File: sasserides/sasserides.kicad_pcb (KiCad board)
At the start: 2 copper layers, 170 x 80 mm, 128 parts, among them J1 Conn_02x16_Odd_Even, Q1 2N7002

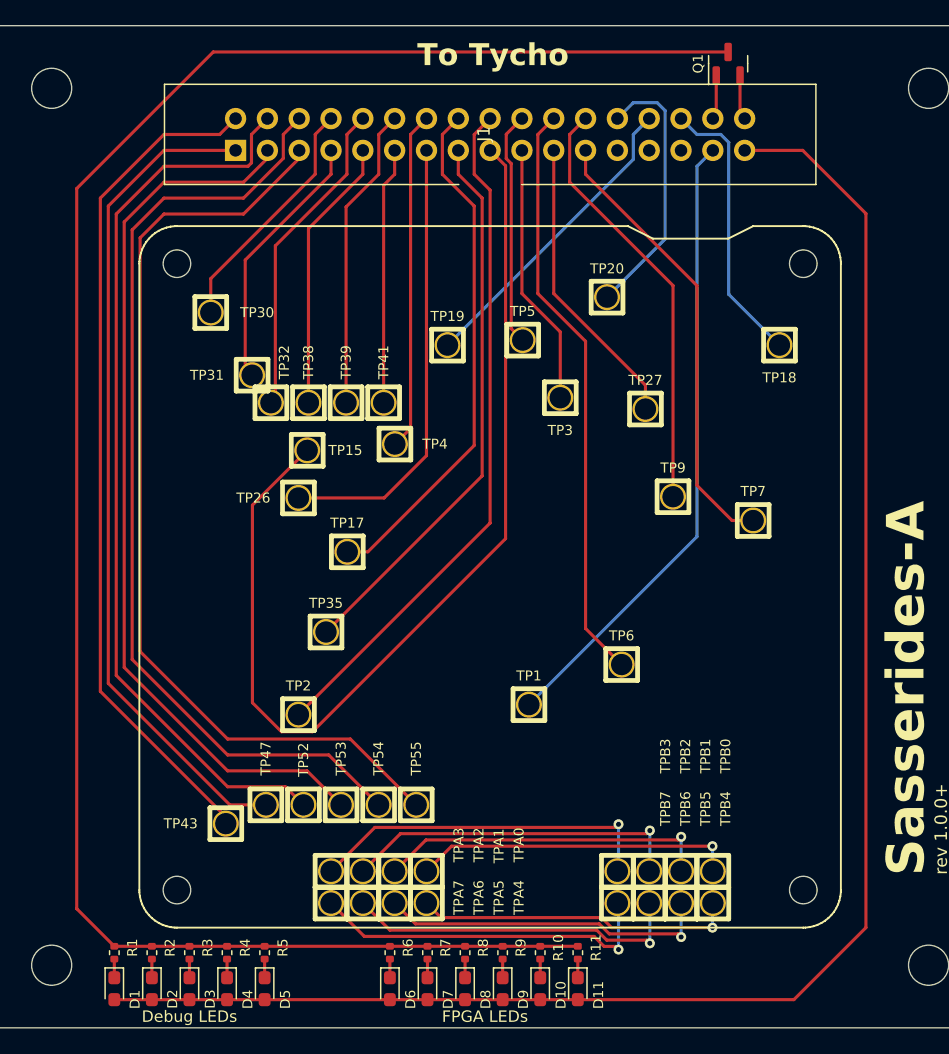
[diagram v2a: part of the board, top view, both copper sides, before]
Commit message: Move Q1 closer to LEDs.
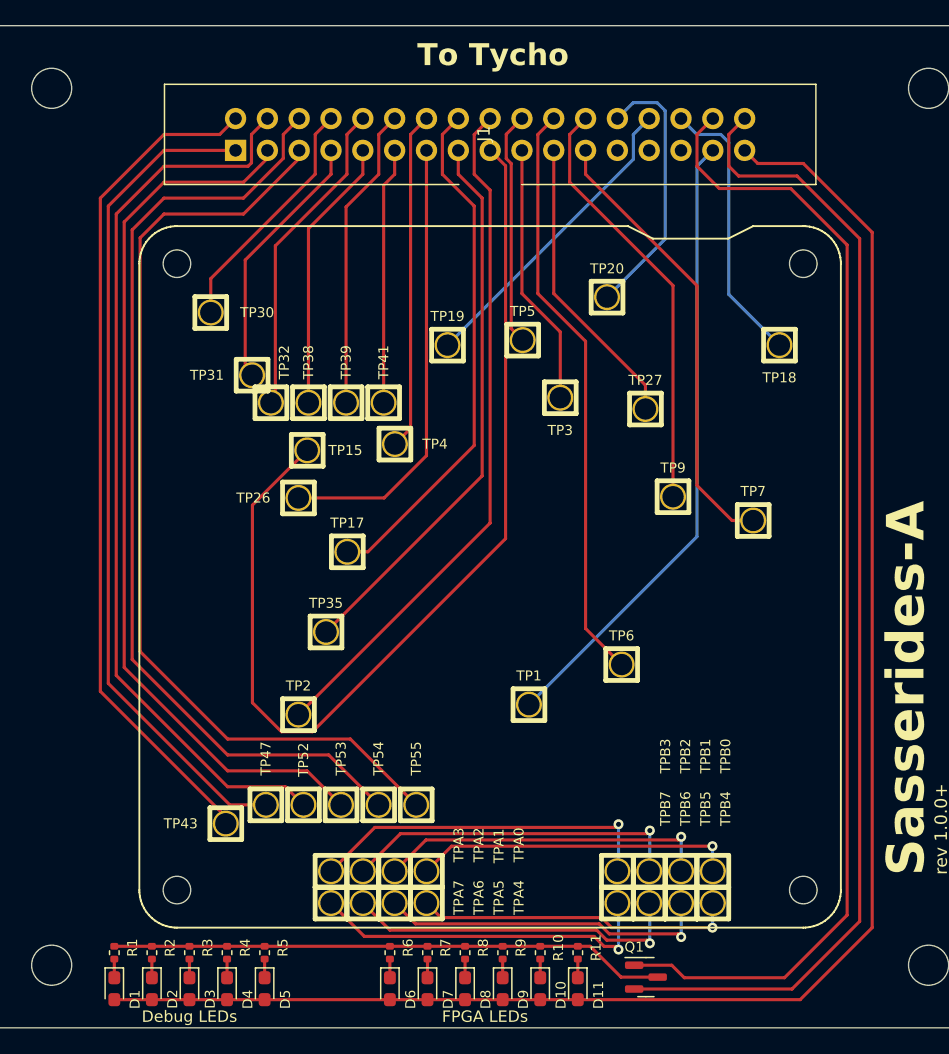
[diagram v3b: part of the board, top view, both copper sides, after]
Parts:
- moved Q1 73.2 mm to (112.4, 135.9), turned to 0 degrees
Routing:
- net Net-(Q1-D): track 155.2 -> 44.4 mm
- net REF_LED_EN: track 3.55 -> 91.9 mm
- net GND: track 3.59 -> 91.9 mm
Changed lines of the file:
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@@
   )
   (footprint "Package_TO_SOT_SMD:SOT-23" (layer "F.Cu")
-    (at 119 63.0375 90)
+    (at 112.4375 135.95)
     (descr "SOT, 3 Pin (https://www.jedec.org/system/files/docs/to-236h.pdf variant AB), generated with kicad-footprint-generator ipc_gullwing_generator.py")
     (tags "SOT TO_SOT_SMD")
@@
     (property "ki_keywords" "N-Channel Switching MOSFET")
     (attr smd)
-    (fp_text reference "Q1" (at 0 -2.4 90) (layer "F.SilkS")
-        (effects (font (size 0.8 0.8) (thickness 0.15)))
-    )
-    (fp_text value "2N7002" (at 0 2.4 90) (layer "F.Fab") hide
+    (fp_text reference "Q1" (at -0.9375 -2.4) (layer "F.SilkS")
+        (effects (font (size 0.8 0.8) (thickness 0.15)))
+    )
+    (fp_text value "2N7002" (at 0 2.4) (layer "F.Fab") hide
         (effects (font (size 1 1) (thickness 0.15)))
     )
-    (fp_text user "${REFERENCE}" (at 0 0 90) (layer "F.Fab")
+    (fp_text user "${REFERENCE}" (at 0 0) (layer "F.Fab")
         (effects (font (size 0.32 0.32) (thickness 0.05)))
     )
@@
     (fp_line (start 0.65 1.45) (end -0.65 1.45)
       (stroke (width 0.1) (type solid)) (layer "F.Fab"))
-    (pad "1" smd roundrect (at -0.9375 -0.95 90) (size 1.475 0.6) (layers "F.Cu" "F.Paste" "F.Mask") (roundrect_rratio 0.25)
+    (pad "1" smd roundrect (at -0.9375 -0.95) (size 1.475 0.6) (layers "F.Cu" "F.Paste" "F.Mask") (roundrect_rratio 0.25)
       (net 44 "REF_LED_EN") (pinfunction "G") (pintype "input"))
-    (pad "2" smd roundrect (at -0.9375 0.95 90) (size 1.475 0.6) (layers "F.Cu" "F.Paste" "F.Mask") (roundrect_rratio 0.25)
+    (pad "2" smd roundrect (at -0.9375 0.95) (size 1.475 0.6) (layers "F.Cu" "F.Paste" "F.Mask") (roundrect_rratio 0.25)
       (net 45 "GND") (pinfunction "S") (pintype "passive"))
-    (pad "3" smd roundrect (at 0.9375 0 90) (size 1.475 0.6) (layers "F.Cu" "F.Paste" "F.Mask") (roundrect_rratio 0.25)
+    (pad "3" smd roundrect (at 0.9375 0) (size 1.475 0.6) (layers "F.Cu" "F.Paste" "F.Mask") (roundrect_rratio 0.25)
       (net 46 "Net-(Q1-D)") (pinfunction "D") (pintype "passive"))
     (model "${KICAD6_3DMODEL_DIR}/Package_TO_SOT_SMD.3dshapes/SOT-23.wrl"
@@
   )
   (segment (start 70 136) (end 70 134.51) (width 0.25) (layer "F.Cu") (net 1))
-  (segment (start 124.25 137.75) (end 130 132) (width 0.25) (layer "F.Cu") (net 2))
-  (segment (start 124.955 69.955) (end 120.32 69.955) (width 0.25) (layer "F.Cu") (net 2))
-  (segment (start 70 137.75) (end 124.25 137.75) (width 0.25) (layer "F.Cu") (net 2))
-  (segment (start 130 132) (end 130 75) (width 0.25) (layer "F.Cu") (net 2))
-  (segment (start 130 75) (end 124.955 69.955) (width 0.25) (layer "F.Cu") (net 2))
+  (segment (start 130.5 76.5) (end 125 71) (width 0.25) (layer "F.Cu") (net 2))
+  (segment (start 124.75 137.75) (end 130.5 132) (width 0.25) (layer "F.Cu") (net 2))
+  (segment (start 121.365 71) (end 120.32 69.955) (width 0.25) (layer "F.Cu") (net 2))
+  (segment (start 125 71) (end 121.365 71) (width 0.25) (layer "F.Cu") (net 2))
+  (segment (start 130.5 132) (end 130.5 76.5) (width 0.25) (layer "F.Cu") (net 2))
+  (segment (start 70 137.75) (end 124.75 137.75) (width 0.25) (layer "F.Cu") (net 2))
   (segment (start 73 136) (end 73 134.51) (width 0.25) (layer "F.Cu") (net 3))
   (segment (start 76 136) (end 76 134.51) (width 0.25) (layer "F.Cu") (net 4))
@@
   (segment (start 117.78 69.955) (end 116.51 71.225) (width 0.25) (layer "B.Cu") (net 43))
   (segment (start 116.51 100.79) (end 103.1 114.2) (width 0.25) (layer "B.Cu") (net 43))
-  (segment (start 118.05 63.975) (end 118.05 67.145) (width 0.25) (layer "F.Cu") (net 44))
-  (segment (start 118.05 67.145) (end 117.78 67.415) (width 0.25) (layer "F.Cu") (net 44))
-  (segment (start 119.95 67.045) (end 120.32 67.415) (width 0.25) (layer "F.Cu") (net 45))
-  (segment (start 119.95 63.975) (end 119.95 67.045) (width 0.25) (layer "F.Cu") (net 45))
-  (segment (start 67 130.49) (end 70 133.49) (width 0.25) (layer "F.Cu") (net 46))
-  (segment (start 67 73) (end 67 130.49) (width 0.25) (layer "F.Cu") (net 46))
-  (segment (start 77.9 62.1) (end 67 73) (width 0.25) (layer "F.Cu") (net 46))
+  (segment (start 116.515 71.22) (end 118.295 73) (width 0.25) (layer "F.Cu") (net 44))
+  (segment (start 123.5 136) (end 115.5 136) (width 0.25) (layer "F.Cu") (net 44))
+  (segment (start 118.295 73) (end 124 73) (width 0.25) (layer "F.Cu") (net 44))
+  (segment (start 116.515 68.68) (end 116.515 71.22) (width 0.25) (layer "F.Cu") (net 44))
+  (segment (start 117.78 67.415) (end 116.515 68.68) (width 0.25) (layer "F.Cu") (net 44))
+  (segment (start 128.5 77.5) (end 128.5 131) (width 0.25) (layer "F.Cu") (net 44))
+  (segment (start 114.5 135) (end 111.5 135) (width 0.25) (layer "F.Cu") (net 44))
+  (segment (start 124 73) (end 128.5 77.5) (width 0.25) (layer "F.Cu") (net 44))
+  (segment (start 115.5 136) (end 114.5 135) (width 0.25) (layer "F.Cu") (net 44))
+  (segment (start 128.5 131) (end 123.5 136) (width 0.25) (layer "F.Cu") (net 44))
+  (segment (start 119.055 71.22) (end 119.055 68.68) (width 0.25) (layer "F.Cu") (net 45))
+  (segment (start 111.5 136.9) (end 124.1 136.9) (width 0.25) (layer "F.Cu") (net 45))
+  (segment (start 124.1 136.9) (end 129.5 131.5) (width 0.25) (layer "F.Cu") (net 45))
+  (segment (start 119.055 68.68) (end 120.32 67.415) (width 0.25) (layer "F.Cu") (net 45))
+  (segment (start 124.5 72) (end 119.835 72) (width 0.25) (layer "F.Cu") (net 45))
+  (segment (start 129.5 131.5) (end 129.5 77) (width 0.25) (layer "F.Cu") (net 45))
+  (segment (start 119.835 72) (end 119.055 71.22) (width 0.25) (layer "F.Cu") (net 45))
+  (segment (start 129.5 77) (end 124.5 72) (width 0.25) (layer "F.Cu") (net 45))
+  (segment (start 113.375 135.95) (end 110.45 135.95) (width 0.25) (layer "F.Cu") (net 46))
+  (segment (start 107.99 133.49) (end 107 133.49) (width 0.25) (layer "F.Cu") (net 46))
   (segment (start 107 133.49) (end 70 133.49) (width 0.25) (layer "F.Cu") (net 46))
-  (segment (start 119 62.1) (end 77.9 62.1) (width 0.25) (layer "F.Cu") (net 46))
+  (segment (start 110.45 135.95) (end 107.99 133.49) (width 0.25) (layer "F.Cu") (net 46))
   (segment (start 96.92 125.5) (end 117.75 125.5) (width 0.25) (layer "F.Cu") (net 47))
   (segment (start 94.92 127.5) (end 96.92 125.5) (width 0.25) (layer "F.Cu") (net 47))

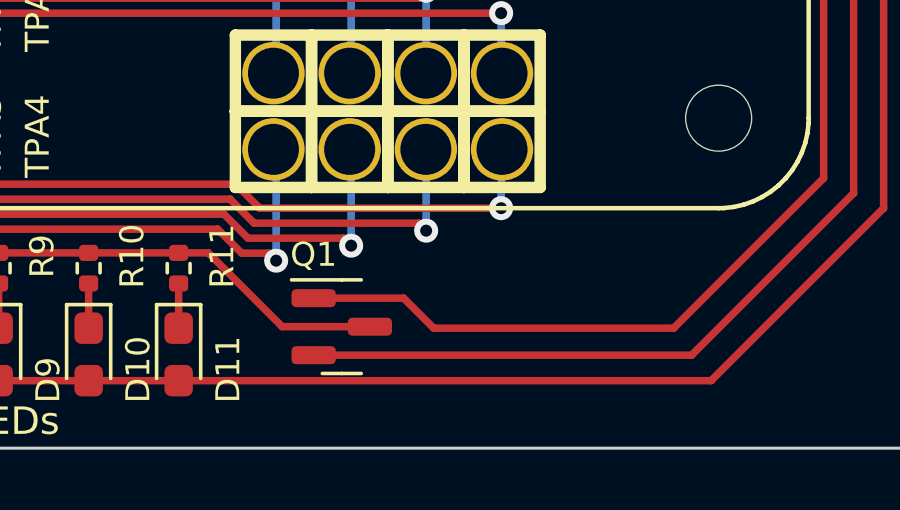
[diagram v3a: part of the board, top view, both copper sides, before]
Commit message: Add 1uF VCC capacitor near LEDs.
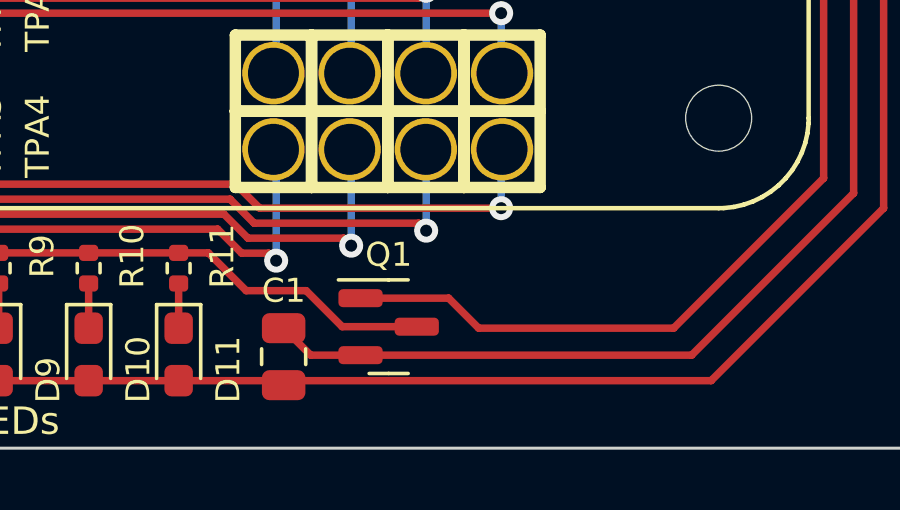
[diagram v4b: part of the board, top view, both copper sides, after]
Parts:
- added C1: 1uF, Capacitor_SMD:C_0805_2012Metric, F.Cu at (110.5, 136.9)
- moved Q1 1.56 mm to (114.0, 135.9)
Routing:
- net REF_LED_EN: track 91.9 -> 90.3 mm
- net Net-(Q1-D): track 44.4 -> 46.0 mm
- net GND: track 91.9 -> 93.3 mm
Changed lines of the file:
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@@
       (net 50 "Net-(TPA3-Pad1)") (pinfunction "1") (pintype "passive"))
   )
+  (footprint "Capacitor_SMD:C_0805_2012Metric" (layer "F.Cu")
+    (at 110.5 136.95 90)
+    (descr "Capacitor SMD 0805 (2012 Metric), square (rectangular) end terminal, IPC_7351 nominal, (Body size source: IPC-SM-782 page 76, https://www.pcb-3d.com/wordpress/wp-content/uploads/ipc-sm-782a_amendment_1_and_2.pdf, https://docs.google.com/spreadsheets/d/1BsfQQcO9C6DZCsRaXUlFlo91Tg2WpOkGARC1WS5S8t0/edit?usp=sharing), generated with kicad-footprint-generator")
+    (tags "capacitor")
+    (property "Sheetfile" "sasserides.kicad_sch")
+    (property "Sheetname" "")
+    (property "ki_description" "Unpolarized capacitor")
+    (property "ki_keywords" "cap capacitor")
+    (attr smd)
+    (fp_text reference "C1" (at 2.2 0) (layer "F.SilkS")
+        (effects (font (size 0.8 0.8) (thickness 0.15)))
+    )
+    (fp_text value "1uF" (at 0 1.68 90) (layer "F.Fab")
+        (effects (font (size 1 1) (thickness 0.15)))
+    )
+    (fp_text user "${REFERENCE}" (at 0 0 90) (layer "F.Fab")
+        (effects (font (size 0.5 0.5) (thickness 0.08)))
+    )
+    (fp_line (start -0.261252 -0.735) (end 0.261252 -0.735)
+      (stroke (width 0.12) (type solid)) (layer "F.SilkS"))
+    (fp_line (start -0.261252 0.735) (end 0.261252 0.735)
+      (stroke (width 0.12) (type solid)) (layer "F.SilkS"))
+    (fp_line (start -1.7 -0.98) (end 1.7 -0.98)
+      (stroke (width 0.05) (type solid)) (layer "F.CrtYd"))
+    (fp_line (start -1.7 0.98) (end -1.7 -0.98)
+      (stroke (width 0.05) (type solid)) (layer "F.CrtYd"))
+    (fp_line (start 1.7 -0.98) (end 1.7 0.98)
+      (stroke (width 0.05) (type solid)) (layer "F.CrtYd"))
+    (fp_line (start 1.7 0.98) (end -1.7 0.98)
+      (stroke (width 0.05) (type solid)) (layer "F.CrtYd"))
+    (fp_line (start -1 -0.625) (end 1 -0.625)
+      (stroke (width 0.1) (type solid)) (layer "F.Fab"))
+    (fp_line (start -1 0.625) (end -1 -0.625)
+      (stroke (width 0.1) (type solid)) (layer "F.Fab"))
+    (fp_line (start 1 -0.625) (end 1 0.625)
+      (stroke (width 0.1) (type solid)) (layer "F.Fab"))
+    (fp_line (start 1 0.625) (end -1 0.625)
+      (stroke (width 0.1) (type solid)) (layer "F.Fab"))
+    (pad "1" smd roundrect (at -0.95 0 90) (size 1 1.45) (layers "F.Cu" "F.Paste" "F.Mask") (roundrect_rratio 0.25)
+      (net 2 "VCC") (pintype "passive"))
+    (pad "2" smd roundrect (at 0.95 0 90) (size 1 1.45) (layers "F.Cu" "F.Paste" "F.Mask") (roundrect_rratio 0.25)
+      (net 45 "GND") (pintype "passive"))
+    (model "${KICAD6_3DMODEL_DIR}/Capacitor_SMD.3dshapes/C_0805_2012Metric.wrl"
+      (offset (xyz 0 0 0))
+      (scale (xyz 1 1 1))
+      (rotate (xyz 0 0 0))
+    )
+  )
   (footprint "tycho:HEADER-1x1-TESTPROBE" (layer "F.Cu")
     (at 177.3 127.5)
@@
   )
   (footprint "Package_TO_SOT_SMD:SOT-23" (layer "F.Cu")
-    (at 112.4375 135.95)
+    (at 114 135.95)
     (descr "SOT, 3 Pin (https://www.jedec.org/system/files/docs/to-236h.pdf variant AB), generated with kicad-footprint-generator ipc_gullwing_generator.py")
     (tags "SOT TO_SOT_SMD")
@@
     (property "ki_keywords" "N-Channel Switching MOSFET")
     (attr smd)
-    (fp_text reference "Q1" (at -0.9375 -2.4) (layer "F.SilkS")
+    (fp_text reference "Q1" (at 0 -2.4) (layer "F.SilkS")
         (effects (font (size 0.8 0.8) (thickness 0.15)))
     )
@@
   (segment (start 117.78 69.955) (end 116.51 71.225) (width 0.25) (layer "B.Cu") (net 43))
   (segment (start 116.51 100.79) (end 103.1 114.2) (width 0.25) (layer "B.Cu") (net 43))
-  (segment (start 116.515 71.22) (end 118.295 73) (width 0.25) (layer "F.Cu") (net 44))
-  (segment (start 123.5 136) (end 115.5 136) (width 0.25) (layer "F.Cu") (net 44))
-  (segment (start 118.295 73) (end 124 73) (width 0.25) (layer "F.Cu") (net 44))
+  (segment (start 124 73) (end 128.5 77.5) (width 0.25) (layer "F.Cu") (net 44))
   (segment (start 116.515 68.68) (end 116.515 71.22) (width 0.25) (layer "F.Cu") (net 44))
-  (segment (start 117.78 67.415) (end 116.515 68.68) (width 0.25) (layer "F.Cu") (net 44))
+  (segment (start 116.515 71.22) (end 118.295 73) (width 0.25) (layer "F.Cu") (net 44))
+  (segment (start 123.5 136) (end 117 136) (width 0.25) (layer "F.Cu") (net 44))
+  (segment (start 117 136) (end 116 135) (width 0.25) (layer "F.Cu") (net 44))
+  (segment (start 116 135) (end 113.0625 135) (width 0.25) (layer "F.Cu") (net 44))
   (segment (start 128.5 77.5) (end 128.5 131) (width 0.25) (layer "F.Cu") (net 44))
-  (segment (start 114.5 135) (end 111.5 135) (width 0.25) (layer "F.Cu") (net 44))
-  (segment (start 124 73) (end 128.5 77.5) (width 0.25) (layer "F.Cu") (net 44))
-  (segment (start 115.5 136) (end 114.5 135) (width 0.25) (layer "F.Cu") (net 44))
   (segment (start 128.5 131) (end 123.5 136) (width 0.25) (layer "F.Cu") (net 44))
-  (segment (start 119.055 71.22) (end 119.055 68.68) (width 0.25) (layer "F.Cu") (net 45))
-  (segment (start 111.5 136.9) (end 124.1 136.9) (width 0.25) (layer "F.Cu") (net 45))
-  (segment (start 124.1 136.9) (end 129.5 131.5) (width 0.25) (layer "F.Cu") (net 45))
+  (segment (start 117.78 67.415) (end 116.515 68.68) (width 0.25) (layer "F.Cu") (net 44))
+  (segment (start 118.295 73) (end 124 73) (width 0.25) (layer "F.Cu") (net 44))
+  (segment (start 129.5 77) (end 124.5 72) (width 0.25) (layer "F.Cu") (net 45))
   (segment (start 119.055 68.68) (end 120.32 67.415) (width 0.25) (layer "F.Cu") (net 45))
+  (segment (start 113.0625 136.9) (end 124.1 136.9) (width 0.25) (layer "F.Cu") (net 45))
   (segment (start 124.5 72) (end 119.835 72) (width 0.25) (layer "F.Cu") (net 45))
+  (segment (start 119.055 71.22) (end 119.055 68.68) (width 0.25) (layer "F.Cu") (net 45))
   (segment (start 129.5 131.5) (end 129.5 77) (width 0.25) (layer "F.Cu") (net 45))
+  (segment (start 111.4 136.9) (end 110.5 136) (width 0.25) (layer "F.Cu") (net 45))
+  (segment (start 124.1 136.9) (end 129.5 131.5) (width 0.25) (layer "F.Cu") (net 45))
   (segment (start 119.835 72) (end 119.055 71.22) (width 0.25) (layer "F.Cu") (net 45))
-  (segment (start 129.5 77) (end 124.5 72) (width 0.25) (layer "F.Cu") (net 45))
-  (segment (start 113.375 135.95) (end 110.45 135.95) (width 0.25) (layer "F.Cu") (net 46))
-  (segment (start 107.99 133.49) (end 107 133.49) (width 0.25) (layer "F.Cu") (net 46))
+  (segment (start 113.0625 136.9) (end 111.4 136.9) (width 0.25) (layer "F.Cu") (net 45))
+  (segment (start 109.25 134.75) (end 107.99 133.49) (width 0.25) (layer "F.Cu") (net 46))
+  (segment (start 112.45 135.95) (end 111.25 134.75) (width 0.25) (layer "F.Cu") (net 46))
+  (segment (start 111.25 134.75) (end 109.25 134.75) (width 0.25) (layer "F.Cu") (net 46))
+  (segment (start 114.9375 135.95) (end 112.45 135.95) (width 0.25) (layer "F.Cu") (net 46))
   (segment (start 107 133.49) (end 70 133.49) (width 0.25) (layer "F.Cu") (net 46))
-  (segment (start 110.45 135.95) (end 107.99 133.49) (width 0.25) (layer "F.Cu") (net 46))
+  (segment (start 107.99 133.49) (end 107 133.49) (width 0.25) (layer "F.Cu") (net 46))
   (segment (start 96.92 125.5) (end 117.75 125.5) (width 0.25) (layer "F.Cu") (net 47))
   (segment (start 94.92 127.5) (end 96.92 125.5) (width 0.25) (layer "F.Cu") (net 47))

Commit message: Give all nets meaningful names.
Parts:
- TP1: value CLK -> ~
- TP15: value nBTN_PROGRAM -> ~
- TP17: value CONTROL_PHY_1V8 -> ~
- TP18: value nBTN_RESET -> ~
- TP19: value MCU_SWDCLK -> ~
- TP2: value AUX_PHY_3V3 -> ~
- TP20: value MCU_SWDIO -> ~
- TP26: value CONTROL_PHY_3V3 -> ~
- TP27: value TARGET_PHY_1V8 -> ~
- TP3: value VCC -> ~
- TP30: value +5V -> ~
- TP31: value D10 Vf -> ~
- TP32: value D11 Vf -> ~
- TP35: value AUX_PHY_1V8 -> ~
- TP38: value D12 Vf -> ~
- TP39: value D13 Vf -> ~
- TP4: value +1V1 -> ~
- TP41: value D14 Vf -> ~
- TP43: value D2 3V3-Vf -> ~
- TP47: value D3 3V3-Vf -> ~
- TP5: value +2V5 -> ~
- TP52: value D4 3V3-Vf -> ~
- TP53: value D5 3V3-Vf -> ~
- TP54: value D6 3V3-Vf -> ~
- TP55: value D7 3V3-Vf -> ~
- TP6: value VCCRAM -> ~
- TP7: value TARGET_A_VBUS -> ~
- TP9: value TARGET_PHY_3V3 -> ~
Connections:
- net Net-(J1-Pin_1) renamed /D3 3V3-Vf
- net Net-(J1-Pin_10) renamed /D11 Vf
- net Net-(J1-Pin_11) renamed /D14 Vf
- net Net-(J1-Pin_12) renamed /D13 Vf
- net Net-(J1-Pin_13) renamed /CONTROL_PHY_3V3
- net Net-(J1-Pin_14) renamed /+1V1
- net Net-(J1-Pin_15) renamed /AUX_PHY_1V8
- net Net-(J1-Pin_16) renamed /CONTROL_PHY_1V8
- net Net-(J1-Pin_17) renamed /~{BTN_PROGRAM}
- net Net-(J1-Pin_18) renamed /AUX_PHY_3V3
- net Net-(J1-Pin_19) renamed /EUT_VCC
- net Net-(J1-Pin_2) renamed /D2 3V3-Vf
- net Net-(J1-Pin_20) renamed /+2V5
- net Net-(J1-Pin_21) renamed /TARGET_PHY_1V8
- net Net-(J1-Pin_22) renamed /VCCRAM
- net Net-(J1-Pin_23) renamed /TARGET_A_VBUS
- net Net-(J1-Pin_24) renamed /TARGET_PHY_3V3
- net Net-(J1-Pin_26) renamed /MCU_SWDIO
- net Net-(J1-Pin_28) renamed /MCU_SWDCLK
- net Net-(J1-Pin_3) renamed /D5 3V3-Vf
- net Net-(J1-Pin_30) renamed /~{BTN_RESET}
- net Net-(J1-Pin_31) renamed /CLK
- net Net-(J1-Pin_4) renamed /D4 3V3-Vf
- net Net-(J1-Pin_5) renamed /D7 3V3-Vf
- net Net-(J1-Pin_6) renamed /D6 3V3-Vf
- net Net-(J1-Pin_7) renamed /D10 Vf
- net Net-(J1-Pin_8) renamed /+5V
- net Net-(J1-Pin_9) renamed /D12 Vf
- net Net-(TPA0-Pad1) renamed /A0B0
- net Net-(TPA1-Pad1) renamed /A1B1
- net Net-(TPA2-Pad1) renamed /A2B2
- net Net-(TPA3-Pad1) renamed /A3B3
- net Net-(TPA4-Pad1) renamed /A4B4
- net Net-(TPA5-Pad1) renamed /A5B5
- net Net-(TPA6-Pad1) renamed /A6B6
- net Net-(TPA7-Pad1) renamed /A7B7
